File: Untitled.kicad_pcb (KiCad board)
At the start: 2 copper layers, 37 x 37 mm, 22 parts, among them J1 Battery Connector, J2 Top Screw Terminal, J3 Bottom Screw Terminal, Q1 Q_NMOS_DGS, Q2 Q_NMOS_DGS, Q3 Q_NMOS_DGS, U1 XIAO-ESP32-S3-SMD, U3 LSM6DSO32, U4 MS5611-01BA

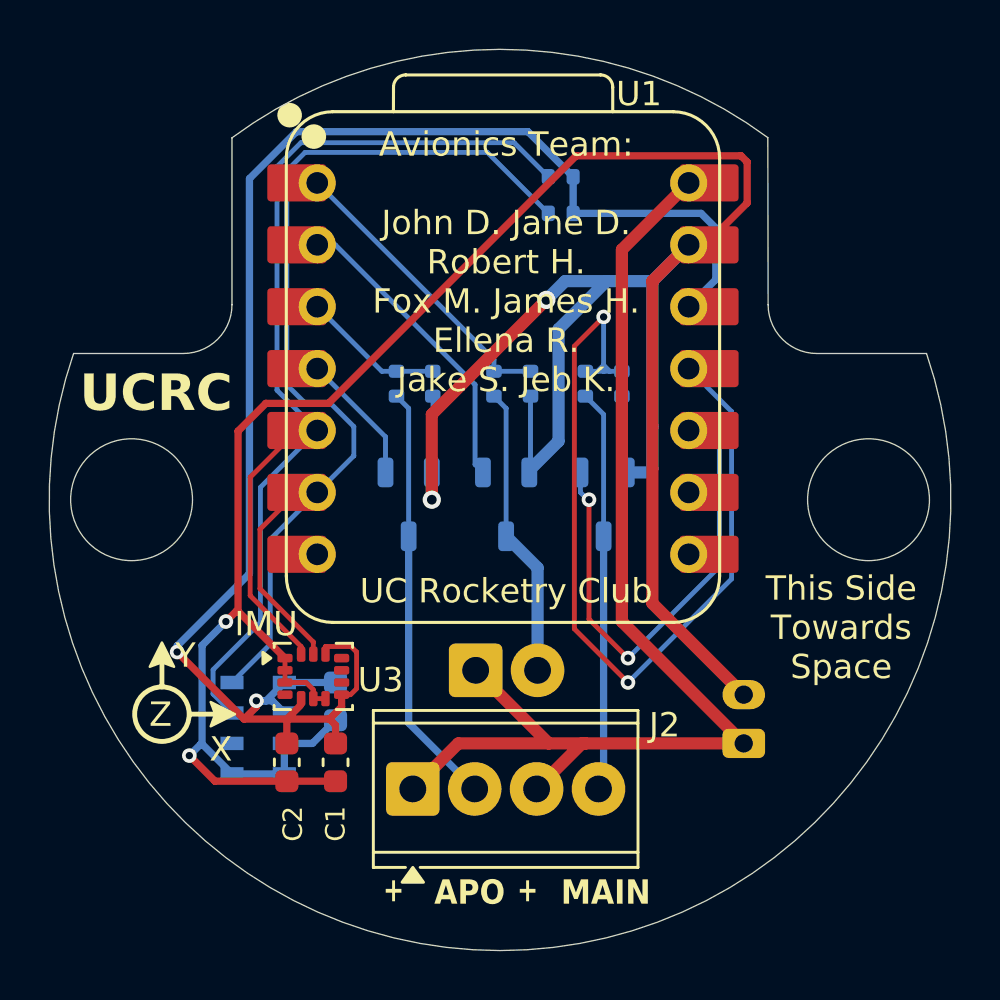
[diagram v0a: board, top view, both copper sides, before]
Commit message: Hole Updates and Initial Names
Updated the threaded rod holes to extend to the PCB edge due to them previously leaving such a small gap near the sides of the holes. Drill footprints still there for now, will be removed in final version. Added initial names for every member of the avionics team in alphabetical order. Updated schematic to reflect current state of PCB connections, specifically with the locations of the pyro pins.
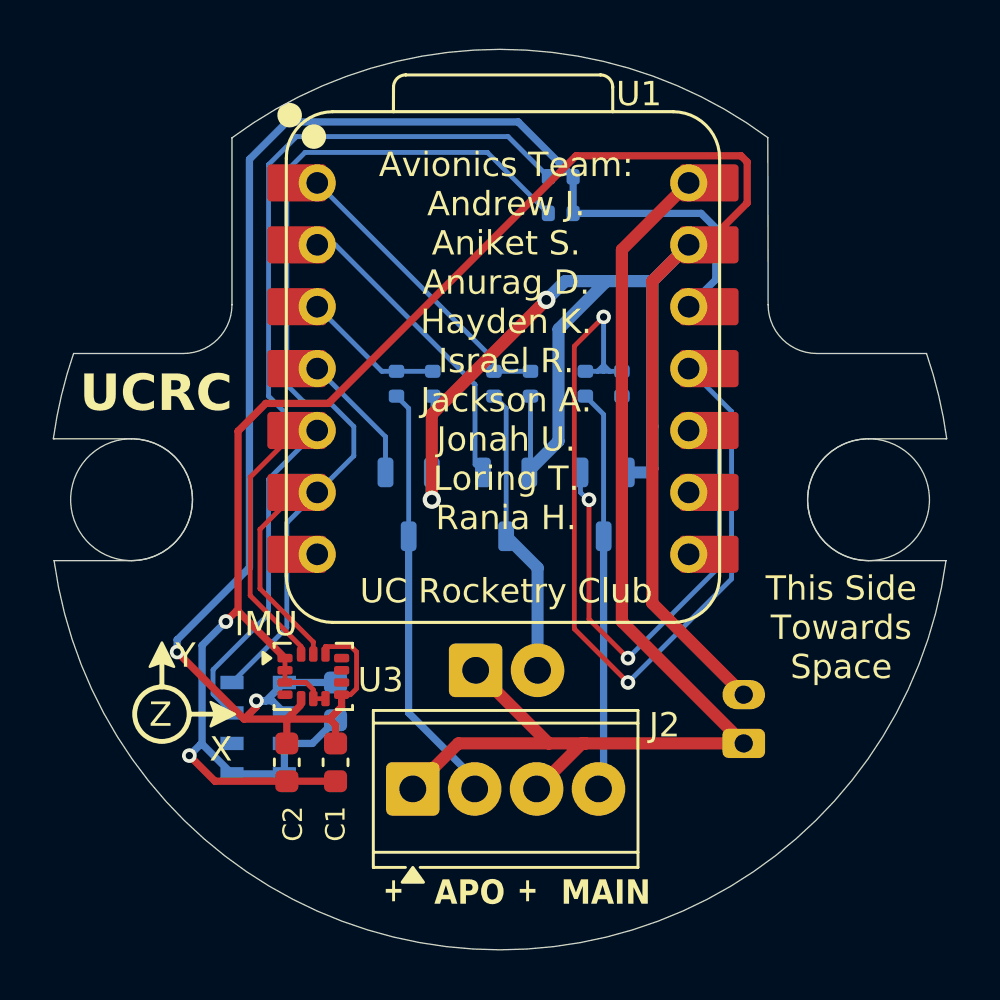
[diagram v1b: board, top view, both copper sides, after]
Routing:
- net /SDA: track 48.2 -> 49.2 mm
- net +3.3V: track 68.0 -> 68.8 mm
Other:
- board size 37 x 37 mm -> 36.7 x 37 mm
- board text added: "Avionics Team: Andrew J. Aniket S. Anurag D. Hayden K. Israel R. Jackson A. Jonah U. Loring T. Rania H."
- board text removed: "Avionics Team: John D. Jane D. Robert H. Fox M. James H. Ellena R. Jake S. Jeb K."
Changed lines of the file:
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@@
 	(net 21 "unconnected-(U3-NC-Pad11)")
 	(net 22 "unconnected-(U4-SDO-Pad6)")
+	(net 23 "unconnected-(U1-GPIO43_A6_D6_TX-Pad7)")
+	(net 24 "unconnected-(U1-GPIO7_A8_D8_SCK-Pad9)")
+	(net 25 "unconnected-(U1-GPIO44_D7_RX-Pad8)")
 	(footprint "Capacitor_SMD:C_0603_1608Metric"
 		(layer "F.Cu")
@@
 			(layers "F.Cu" "F.Mask")
 			(roundrect_rratio 0.1)
-			(net 15 "unconnected-(U1-GPIO43_A6_D6_TX-Pad7)_1")
+			(net 23 "unconnected-(U1-GPIO43_A6_D6_TX-Pad7)")
 			(pinfunction "GPIO43_A6_D6_TX")
 			(pintype "passive+no_connect")
@@
 			(layers "F.Cu" "F.Mask")
 			(roundrect_rratio 0.1)
-			(net 17 "unconnected-(U1-GPIO44_D7_RX-Pad8)_1")
+			(net 25 "unconnected-(U1-GPIO44_D7_RX-Pad8)")
 			(pinfunction "GPIO44_D7_RX")
 			(pintype "passive+no_connect")
@@
 			(layers "F.Cu" "F.Mask")
 			(roundrect_rratio 0.1)
-			(net 16 "unconnected-(U1-GPIO7_A8_D8_SCK-Pad9)_1")
+			(net 24 "unconnected-(U1-GPIO7_A8_D8_SCK-Pad9)")
 			(pinfunction "GPIO7_A8_D8_SCK")
 			(pintype "passive+no_connect")
@@
 		(layer "F.SilkS")
 	)
+	(gr_arc
+		(start 224.3 70)
+		(mid 206 85.969976)
+		(end 187.7 70)
+		(stroke
+			(width 0.05)
+			(type default)
+		)
+		(layer "Edge.Cuts")
+	)
 	(gr_line
 		(start 223.5 61.5)
@@
 	)
 	(gr_arc
+		(start 221.12 70)
+		(mid 218.62 67.5)
+		(end 221.12 65)
+		(stroke
+			(width 0.05)
+			(type solid)
+		)
+		(layer "Edge.Cuts")
+	)
+	(gr_arc
 		(start 219 61.5)
 		(mid 217.585786 60.914214)
@@
 		(layer "Edge.Cuts")
 	)
+	(gr_arc
+		(start 187.670252 64.995936)
+		(mid 188.000053 63.227776)
+		(end 188.5 61.5)
+		(stroke
+			(width 0.05)
+			(type default)
+		)
+		(layer "Edge.Cuts")
+	)
+	(gr_line
+		(start 187.669699 64.999995)
+		(end 187.7 65)
+		(stroke
+			(width 0.05)
+			(type default)
+		)
+		(layer "Edge.Cuts")
+	)
+	(gr_arc
+		(start 190.88 65)
+		(mid 193.38 67.5)
+		(end 190.88 70)
+		(stroke
+			(width 0.05)
+			(type solid)
+		)
+		(layer "Edge.Cuts")
+	)
+	(gr_line
+		(start 221.12 65)
+		(end 224.3 65)
+		(stroke
+			(width 0.05)
+			(type default)
+		)
+		(layer "Edge.Cuts")
+	)
 	(gr_line
 		(start 217 59.5)
@@
 		(layer "Edge.Cuts")
 	)
+	(gr_line
+		(start 190.88 65)
+		(end 187.7 65)
+		(stroke
+			(width 0.05)
+			(type default)
+		)
+		(layer "Edge.Cuts")
+	)
+	(gr_line
+		(start 221.12 70)
+		(end 224.3 70)
+		(stroke
+			(width 0.05)
+			(type default)
+		)
+		(layer "Edge.Cuts")
+	)
+	(gr_line
+		(start 224.330302 64.999995)
+		(end 224.3 65)
+		(stroke
+			(width 0.05)
+			(type default)
+		)
+		(layer "Edge.Cuts")
+	)
+	(gr_line
+		(start 190.88 70)
+		(end 187.7 70)
+		(stroke
+			(width 0.05)
+			(type default)
+		)
+		(layer "Edge.Cuts")
+	)
 	(gr_arc
 		(start 223.5 61.5)
-		(mid 206 86)
-		(end 188.5 61.5)
+		(mid 223.999947 63.227776)
+		(end 224.329748 64.995936)
 		(stroke
 			(width 0.05)
@@
 		)
 	)
-	(gr_text "Avionics Team:\n\nJohn D. Jane D.\nRobert H.\nFox M. James H.\nEllena R.\nJake S. Jeb K."
-		(at 206.25 57.75 0)
+	(gr_text "Avionics Team:\nAndrew J.\nAniket S.\nAnurag D.\nHayden K. \nIsrael R.\nJackson A.\nJonah U. \nLoring T.\nRania H."
+		(at 206.25 61 0)
 		(layer "F.SilkS")
 		(effects
@@
 	)
 	(segment
-		(start 195.71766 70.53234)
-		(end 192.75 73.5)
+		(start 206.75 52)
+		(end 197.25 52)
 		(width 0.3)
 		(layer "B.Cu")
@@
 	)
 	(segment
-		(start 197.645435 52.398)
-		(end 195.71766 54.325775)
+		(start 209 54.25)
+		(end 206.75 52)
 		(width 0.3)
 		(layer "B.Cu")
@@
 	)
 	(segment
-		(start 207.148 52.398)
-		(end 197.645435 52.398)
+		(start 196 75.75)
+		(end 196.4 75.75)
 		(width 0.3)
 		(layer "B.Cu")
@@
 	)
 	(segment
-		(start 196 75.75)
-		(end 196.4 75.75)
+		(start 195.71766 53.53234)
+		(end 195.71766 70.28234)
 		(width 0.3)
 		(layer "B.Cu")
@@
 	)
 	(segment
-		(start 209 54.25)
-		(end 207.148 52.398)
+		(start 195.71766 70.28234)
+		(end 192.75 73.25)
 		(width 0.3)
 		(layer "B.Cu")
@@
 	)
 	(segment
-		(start 195.71766 54.325775)
-		(end 195.71766 70.53234)
-		(width 0.3)
-		(layer "B.Cu")
-		(net 1)
-	)
-	(segment
-		(start 192.75 73.5)
-		(end 192.75 73.75)
+		(start 214.853 58.467)
+		(end 214.853 56.353)
 		(width 0.3)
 		(layer "B.Cu")
@@
 	)
 	(segment
-		(start 214.853 58.467)
-		(end 214.853 56.353)
+		(start 196.4 75.75)
+		(end 197.15 75)
 		(width 0.3)
 		(layer "B.Cu")
@@
 	)
 	(segment
-		(start 196.4 75.75)
-		(end 197.15 75)
+		(start 192.75 73.25)
+		(end 192.75 73.75)
 		(width 0.3)
 		(layer "B.Cu")
@@
 	)
 	(segment
+		(start 197.25 52)
+		(end 195.71766 53.53234)
+		(width 0.3)
+		(layer "B.Cu")
+		(net 1)
+	)
+	(segment
 		(start 212.25 58.53)
 		(end 213.74 57.04)
@@
 	)
 	(segment
-		(start 202.25 63.75)
-		(end 202.25 69)
-		(width 0.2)
+		(start 204.96 79.3675)
+		(end 204.96 78.96)
+		(width 0.3)
 		(layer "B.Cu")
 		(net 4)
 	)
 	(segment
-		(start 202.25 76.6575)
-		(end 202.25 69)
+		(start 204.96 78.96)
+		(end 202.25 76.25)
 		(width 0.3)
 		(layer "B.Cu")
@@
 	)
 	(segment
-		(start 204.96 79.3675)
-		(end 202.25 76.6575)
+		(start 202.25 63.75)
+		(end 202.25 69)
+		(width 0.2)
+		(layer "B.Cu")
+		(net 4)
+	)
+	(segment
+		(start 202.25 76.25)
+		(end 202.25 69)
 		(width 0.3)
 		(layer "B.Cu")
@@
 	)
 	(segment
-		(start 197.998345 53.25)
-		(end 197.25 53.998345)
+		(start 197.25 68.45)
+		(end 198.5 67.2)
 		(width 0.2)
 		(layer "B.Cu")
@@
 	)
 	(segment
-		(start 197.25 53.998345)
-		(end 197.25 62.78731)
+		(start 197.25 72.75)
+		(end 197.25 68.45)
 		(width 0.2)
 		(layer "B.Cu")
@@
 	)
 	(segment
-		(start 196.56966 73.43034)
-		(end 196.56966 69.13034)
+		(start 197.998345 53.25)
+		(end 197.25 53.998345)
+		(width 0.2)
+		(layer "B.Cu")
+		(net 10)
+	)
+	(segment
+		(start 197.25 53.998345)
+		(end 197.25 62.78731)
 		(width 0.2)
 		(layer "B.Cu")
@@
 	)
 	(segment
-		(start 197.96269 63.5)
-		(end 199 63.5)
+		(start 195 75)
+		(end 197.25 72.75)
 		(width 0.2)
 		(layer "B.Cu")
@@
 	)
 	(segment
-		(start 195 75)
-		(end 196.56966 73.43034)
+		(start 197.96269 63.5)
+		(end 199 63.5)
 		(width 0.2)
 		(layer "B.Cu")
@@
 	)
 	(segment
-		(start 196.56966 69.13034)
-		(end 198.5 67.2)
-		(width 0.2)
-		(layer "B.Cu")
-		(net 10)
-	)
-	(segment
 		(start 199 63.5)
 		(end 200 64.5)
@@
 	)
 	(segment
-		(start 196.849 53.832245)
-		(end 196.849 63.009)
+		(start 207.98 54.25)
+		(end 206.33 52.6)
 		(width 0.2)
 		(layer "B.Cu")
@@
 	)
 	(segment
-		(start 196.849 63.009)
-		(end 198.5 64.66)
+		(start 194.224 75.474)
+		(end 194.224 74.47634)
 		(width 0.2)
 		(layer "B.Cu")
@@
 	)
 	(segment
-		(start 207.98 54.25)
-		(end 206.579 52.849)
+		(start 196.5 63.25)
+		(end 197.91 64.66)
 		(width 0.2)
 		(layer "B.Cu")
@@
 	)
 	(segment
-		(start 196.16866 72.53168)
-		(end 196.16866 66.99134)
+		(start 197.65 52.6)
+		(end 196.5 53.75)
 		(width 0.2)
 		(layer "B.Cu")
@@
 	)
 	(segment
-		(start 195 76.25)
-		(end 194.224 75.474)
+		(start 206.33 52.6)
+		(end 197.65 52.6)
 		(width 0.2)
 		(layer "B.Cu")
@@
 	)
 	(segment
-		(start 194.224 74.47634)
-		(end 196.16866 72.53168)
+		(start 197.91 64.66)
+		(end 198.5 64.66)
 		(width 0.2)
 		(layer "B.Cu")
@@
 	)
 	(segment
-		(start 196.16866 66.99134)
+		(start 195 76.25)
+		(end 194.224 75.474)
+		(width 0.2)
+		(layer "B.Cu")
+		(net 11)
+	)
+	(segment
+		(start 196.5 66.66)
 		(end 198.5 64.66)
 		(width 0.2)
@@
 	)
 	(segment
-		(start 197.832245 52.849)
-		(end 196.849 53.832245)
+		(start 196.5 72.20034)
+		(end 196.5 66.66)
 		(width 0.2)
 		(layer "B.Cu")
@@
 	)
 	(segment
-		(start 194.224 75.474)
-		(end 194.224 74.47634)
+		(start 196.5 53.75)
+		(end 196.5 63.25)
 		(width 0.2)
 		(layer "B.Cu")
@@
 	)
 	(segment
-		(start 206.579 52.849)
-		(end 197.832245 52.849)
+		(start 194.224 74.47634)
+		(end 196.5 72.20034)
 		(width 0.2)
 		(layer "B.Cu")

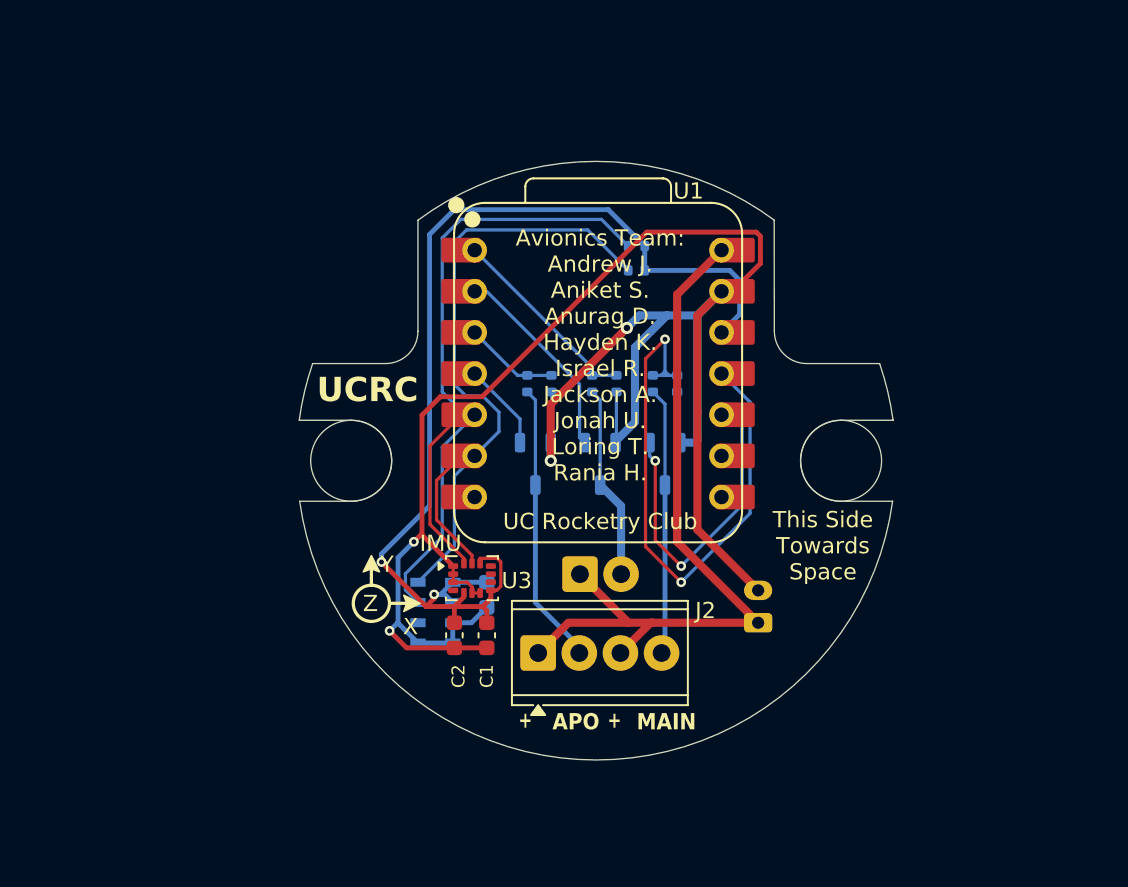
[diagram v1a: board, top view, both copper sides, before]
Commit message: New Rgs Resistors and Ground Pour
Added a set of 3 new resistors that bridge the gate of the MOSFETs to ground with a 4.7 ohm resistor, which can help filter out any unintentional activation of the MOSFET due to interference (detailed in datasheet). Also added a ground pour to the PCB for added EMI resistance and overall higher performance.
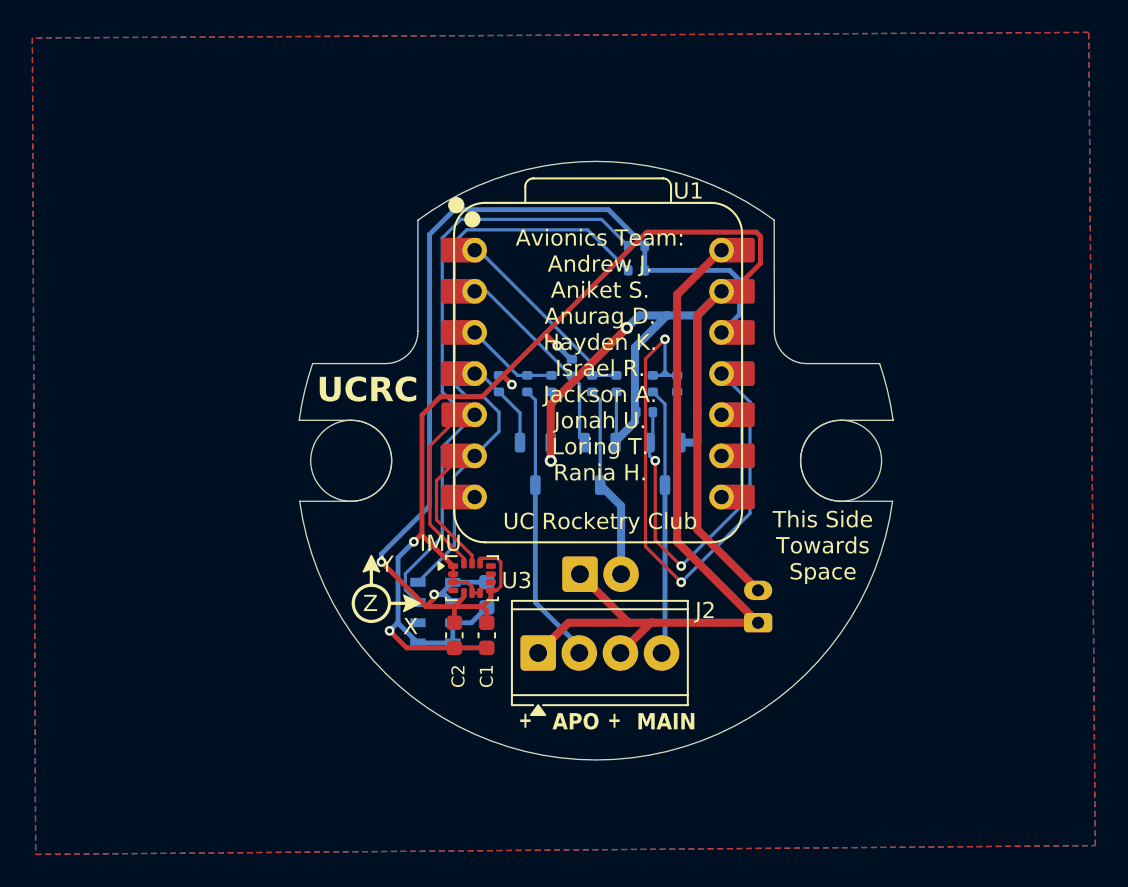
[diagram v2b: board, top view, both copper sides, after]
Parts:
- added R10: 4.7, Resistor_SMD:R_0402_1005Metric, B.Cu at (200.0, 62.7)
- added R11: 4.7, Resistor_SMD:R_0402_1005Metric, B.Cu at (204.5, 61.7)
- added R9: 4.7, Resistor_SMD:R_0402_1005Metric, B.Cu at (209.0, 64.5)
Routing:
- net -BATT: track 130.8 -> 134.9 mm, vias 4 -> 6
- net /IGNIT 2: track 20.3 -> 22.2 mm
- added copper zone on B.Cu, net -BATT
- added copper zone on F.Cu, net -BATT
